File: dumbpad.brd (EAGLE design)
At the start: 98 x 79.5 mm, 36 parts

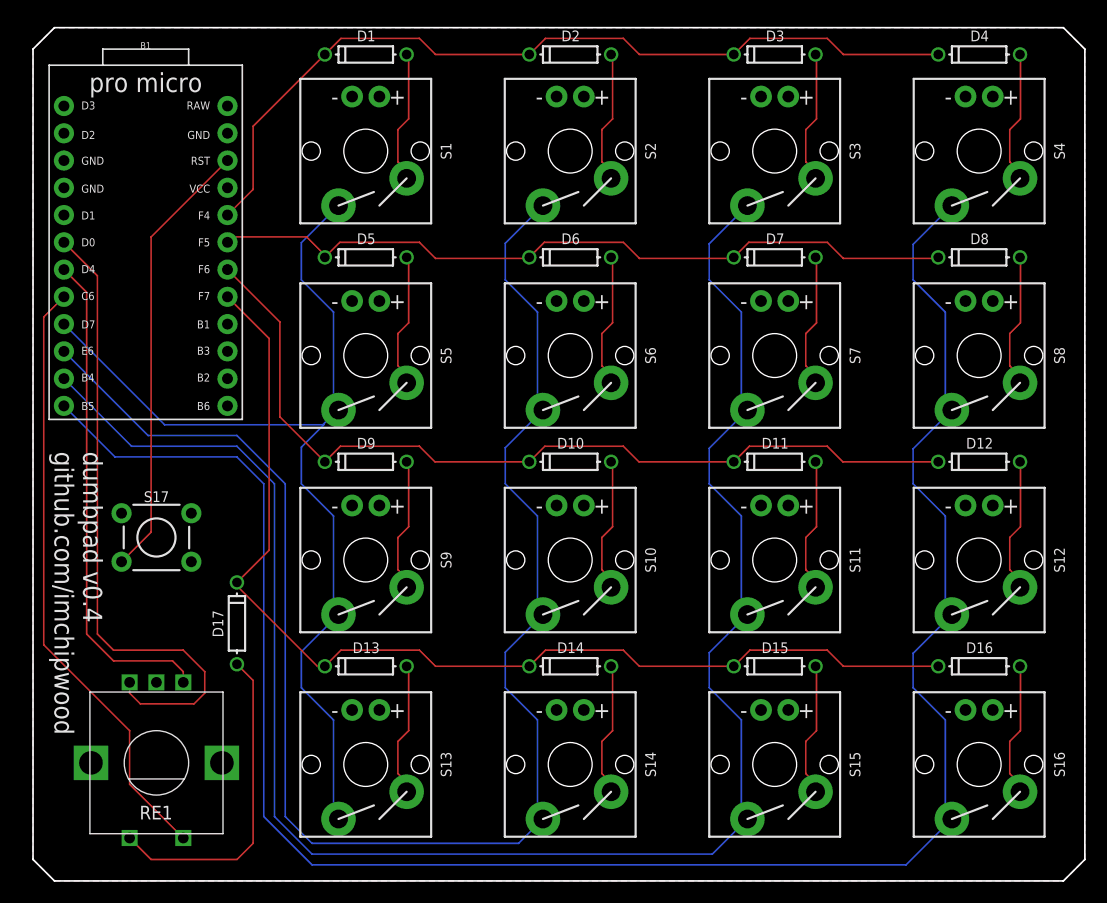
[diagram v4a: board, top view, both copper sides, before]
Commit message: v0.4 done - moved diodes to right side of switches for cleaner routing. Adjusted dimension slightly to give more room around switches so keycaps don't hang over the sides
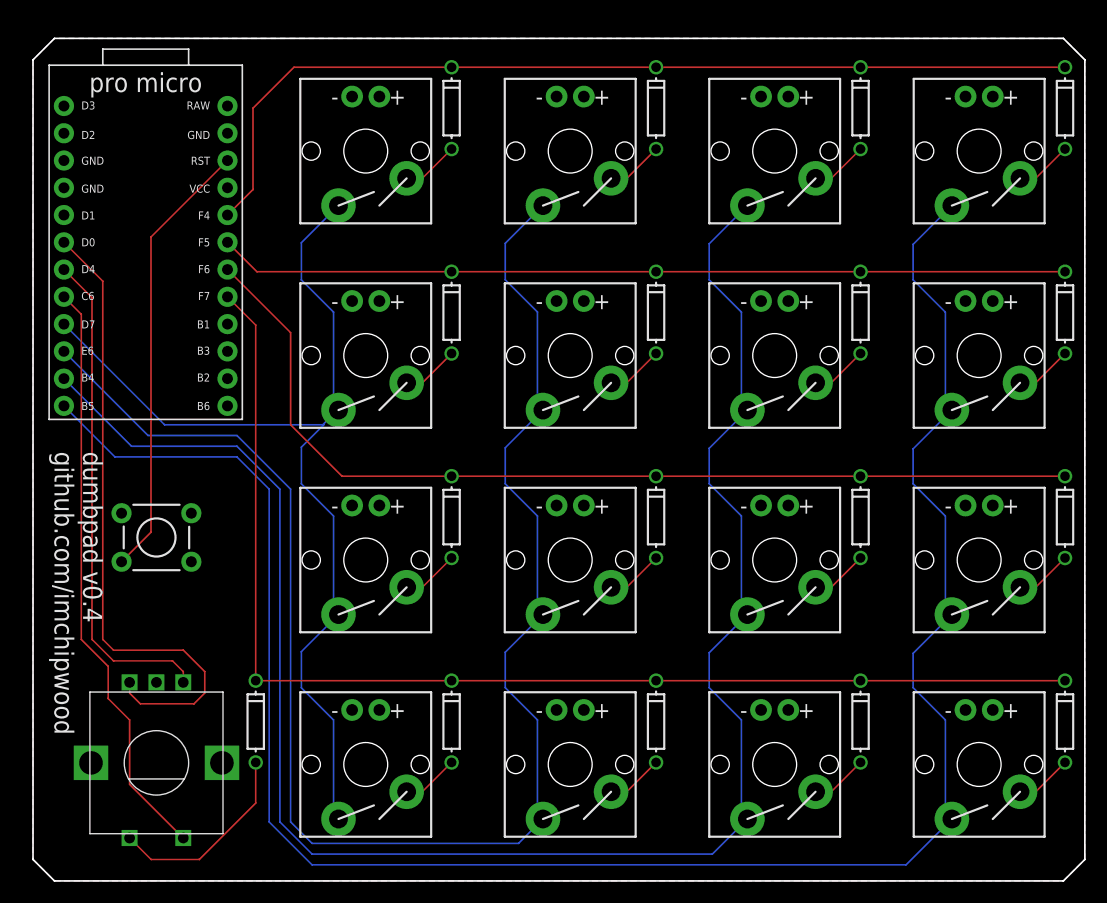
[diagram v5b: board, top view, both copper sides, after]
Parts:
- moved D13 9.51 mm to (40.0, 14.8), turned to 90 degrees
- moved D14 9.51 mm to (59.0, 14.8), turned to 90 degrees
- moved D15 9.51 mm to (78.1, 14.8), turned to 90 degrees
- moved D16 9.51 mm to (97.2, 14.8), turned to 90 degrees
- moved D10 9.51 mm to (59.0, 33.9), turned to 90 degrees
- moved D11 9.51 mm to (78.1, 33.9), turned to 90 degrees
- moved D12 9.51 mm to (97.2, 33.9), turned to 90 degrees
- moved D5 9.51 mm to (40.0, 53.0), turned to 90 degrees
- moved D6 9.51 mm to (59.0, 53.0), turned to 90 degrees
- moved D7 9.51 mm to (78.1, 53.0), turned to 90 degrees
- moved D8 9.51 mm to (97.2, 53.0), turned to 90 degrees
- moved D9 9.51 mm to (40.0, 33.9), turned to 90 degrees
- moved D1 9.43 mm to (40.0, 72.0), turned to 90 degrees
- moved D2 9.43 mm to (59.0, 72.0), turned to 90 degrees
- moved D3 9.43 mm to (78.1, 72.0), turned to 90 degrees
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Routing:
- net N$10: track 30.3 -> 18.5 mm
- net ROW3: track 101.9 -> 112.2 mm
- net ROW2: track 82.4 -> 91.0 mm
- net ROW0: track 79.6 -> 88.2 mm
- net ROW1: track 71.1 -> 79.2 mm
- net N$8: track 12.5 -> 5.32 mm
- net N$7: track 12.5 -> 5.32 mm
- net N$9: track 12.5 -> 5.32 mm
- net N$14: track 12.5 -> 5.32 mm
- net N$13: track 12.5 -> 5.32 mm
- net N$12: track 12.5 -> 5.32 mm
- net N$19: track 12.5 -> 5.32 mm
- net N$18: track 12.5 -> 5.32 mm
- net N$17: track 12.5 -> 5.32 mm
- net N$6: track 12.5 -> 5.32 mm
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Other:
- board size 98 x 79.5 mm -> 98 x 78.5 mm

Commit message: more tweaks to v4 for A E S T H E T I C
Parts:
- moved D1 4.00 mm to (40.0, 68.0)
- moved D10 4.00 mm to (59.0, 29.9)
- moved D11 4.00 mm to (78.1, 29.9)
- moved D12 4.00 mm to (97.2, 29.9)
- moved D13 4.00 mm to (40.0, 10.8)
- moved D14 4.00 mm to (59.0, 10.8)
- moved D15 4.00 mm to (78.1, 10.8)
- moved D16 4.00 mm to (97.2, 10.8)
- moved D17 4.00 mm to (21.8, 10.8)
- moved D2 4.00 mm to (59.0, 68.0)
- moved D3 4.00 mm to (78.1, 68.0)
- moved D4 4.00 mm to (97.2, 68.0)
- moved D5 4.00 mm to (40.0, 49.0)
- moved D6 4.00 mm to (59.0, 49.0)
- moved D7 4.00 mm to (78.1, 49.0)
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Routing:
- net ROW3: track 112.2 -> 126.3 mm
- net ROW2: track 91.0 -> 102.0 mm
- net ROW1: track 79.2 -> 89.1 mm
- net ROW0: track 88.2 -> 95.7 mm
- net N$10: track 18.5 -> 14.7 mm
- net COL1: track 93.9 -> 92.6 mm
- net RESET: track 41.5 -> 42.7 mm
- net COL0: track 55.0 -> 55.9 mm
- net ENCODER_L0: track 46.3 -> 47.1 mm
- net N$7: track 5.32 -> 4.72 mm
- net N$2: track 5.32 -> 4.72 mm
- net N$8: track 5.32 -> 4.72 mm
- net N$6: track 5.32 -> 4.72 mm
- net N$3: track 5.32 -> 4.72 mm
- net N$1: track 5.32 -> 4.72 mm
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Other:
- board size 98 x 78.5 mm -> 97 x 78.5 mm

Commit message: who doesn't like LEDs
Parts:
- added D18, D19: (no value), SparkFun-LED:LED_3MM
- added LOGO1: OSHW-LOGOL, SparkFun-Aesthetics:OSHW-LOGO-L
- added R1, R2: 330, SparkFun-Resistors:AXIAL-0.3
- moved S17 2.90 mm to (10.5, 29.9)
- moved B1 2.00 mm to (10.5, 59.5)
- moved D12 2.00 mm to (95.2, 29.9)
- moved D16 2.00 mm to (95.2, 10.8)
- moved D17 2.00 mm to (19.8, 10.8)
- moved D4 2.00 mm to (95.2, 68.0)
- moved D8 2.00 mm to (95.2, 49.0)
- moved RE1 2.00 mm to (10.5, 11.0)
- moved S1 2.00 mm to (30.0, 68.0)
- moved S10 2.00 mm to (49.0, 29.9)
- moved S11 2.00 mm to (68.1, 29.9)
- moved S12 2.00 mm to (87.2, 29.9)
- moved S13 2.00 mm to (30.0, 10.8)
- moved S14 2.00 mm to (49.0, 10.8)
- moved S15 2.00 mm to (68.1, 10.8)
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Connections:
- new net LED0: B1.16, R1.P$2
- new net LED1: B1.15, R2.P$2
- new net N$15: D19.A, R2.P$1
- new net N$5: D18.A, R1.P$1
- net GND: now also D18.K, D19.K
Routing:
- net N$5: track 0.00 -> 21.9 mm
- net LED0: track 0.00 -> 21.4 mm
- net LED1: track 0.00 -> 19.3 mm
- net N$15: track 0.00 -> 16.4 mm
- net RESET: track 42.7 -> 44.9 mm
- net ROW0: track 95.7 -> 97.4 mm
- net N$8: track 4.72 -> 6.24 mm
- net N$7: track 4.72 -> 6.24 mm
- net N$3: track 4.72 -> 6.24 mm
- net N$2: track 4.72 -> 6.24 mm
- net N$18: track 4.72 -> 6.24 mm
- net N$17: track 4.72 -> 6.24 mm
- net N$13: track 4.72 -> 6.24 mm
- net N$12: track 4.72 -> 6.24 mm
- net N$9: track 4.72 -> 6.24 mm
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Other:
- board text added: "dumbpad v0.5 github.com/imchipwood"
- board text removed: "dumbpad v0.4 github.com/imchipwood"

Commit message: final touches to v0.5
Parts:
- removed S17: MOMENTARY-SWITCH-SPST-PTH-6.0MM, SparkFun-Switches:TACTILE_SWITCH_PTH_6.0MM
- moved R1 12.4 mm to (10.5, 37.0), turned to 180 degrees
- moved R2 8.49 mm to (10.5, 34.5), turned to 180 degrees
- moved D18 6.71 mm to (8.00, 30.5), turned to 270 degrees
- moved D19 6.71 mm to (13.0, 30.5), turned to 270 degrees
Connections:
- net GND: no longer S17.1
- net RESET: no longer S17.3
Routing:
- net RESET: track 44.9 -> 0.00 mm
- net N$5: track 21.9 -> 8.48 mm
- net N$15: track 16.4 -> 3.27 mm
- net LED0: track 21.4 -> 19.8 mm
- net ENCODER_L0: track 47.1 -> 48.4 mm
- net ENCODER_L1: track 60.6 -> 61.8 mm
- net COL0: track 55.9 -> 57.1 mm
